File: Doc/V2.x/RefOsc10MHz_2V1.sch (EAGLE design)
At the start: 81 parts, among them CON1 TYCO-AMP_USBUSB-B_SMT, CON2 HEADER-2X5SMD, CON3 SD-73100-0105, CON4 AVR-ISP-6SMD, CON5 AVR-JTAG-10SMD, CON6 HEADER-2X3SMD, CON7 MCX-J-P-X-RA-SM1, IC1 ATmega328-P, IC2 LC4032V_XXT44, IC3 74HCT221D, IC6 LM2831YMF, IC7 CFPT-141, IC8 712-RXM-GNSS-TM-B, U5 OPA354

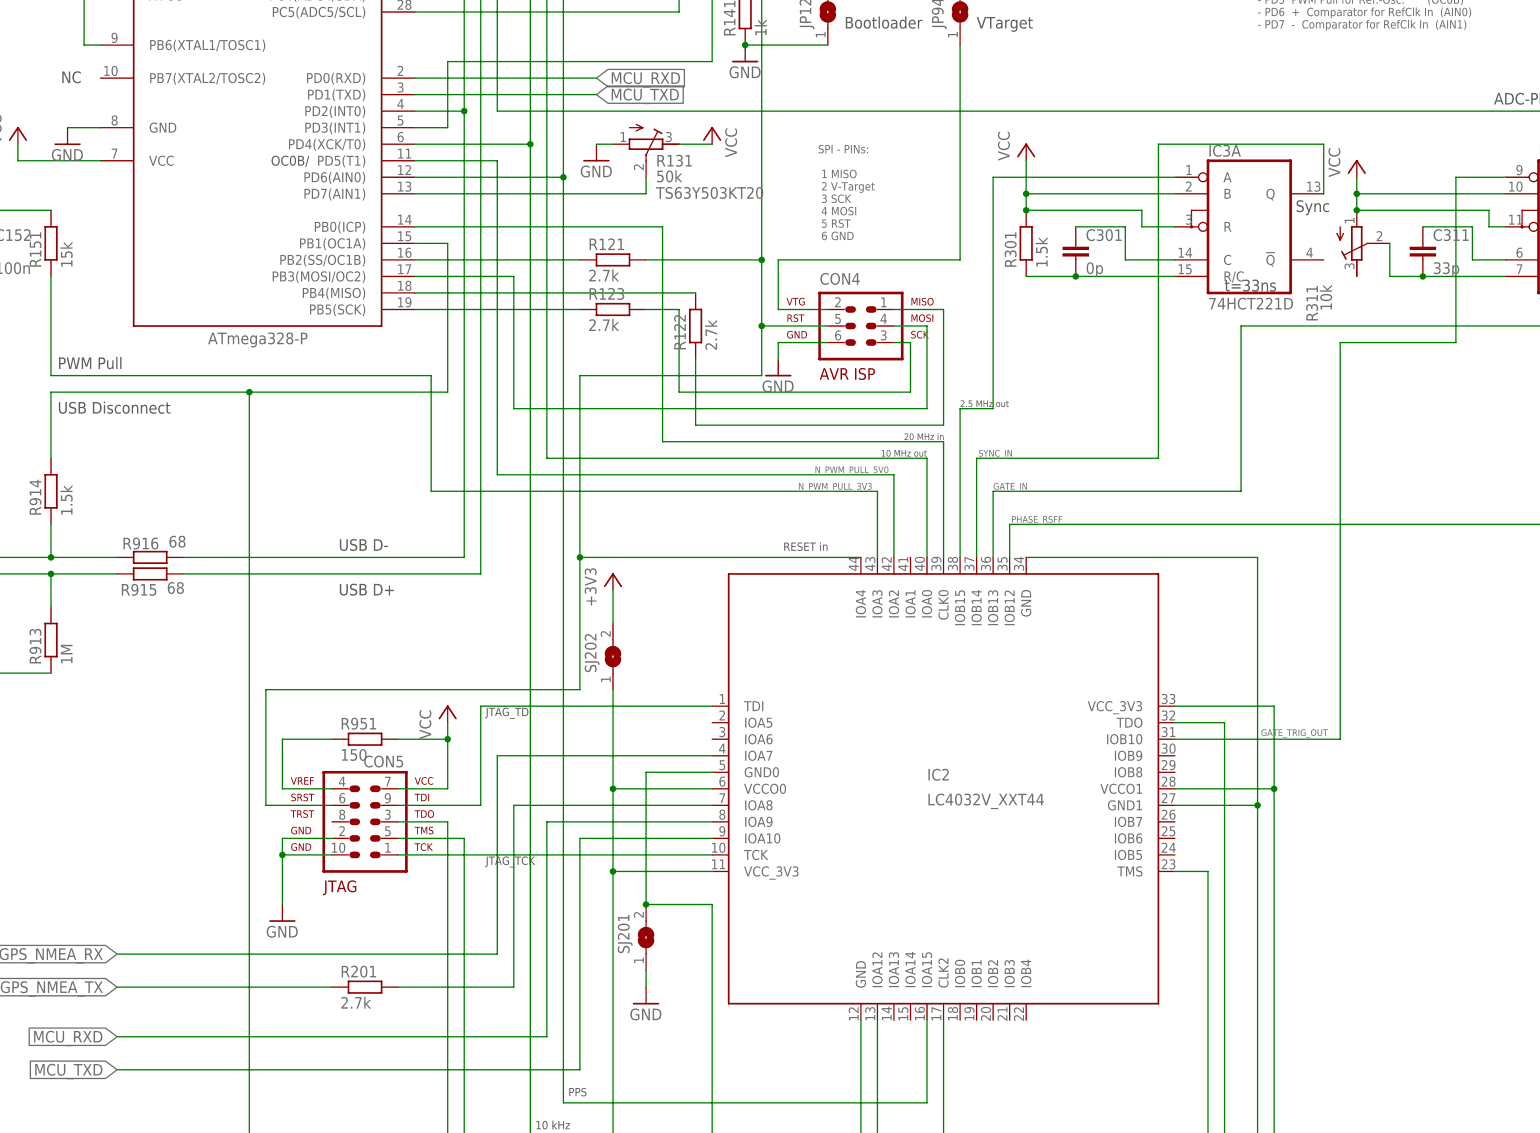
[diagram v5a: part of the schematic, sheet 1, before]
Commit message: avr_DF4IAH_Bootloader - Doc - Eagle: V2.1 - PWM pull signal via CPLD for clamping signals to defined values. AVR controller @ USB is not voltage regulated, the PWM output is therefore variable in its output voltage
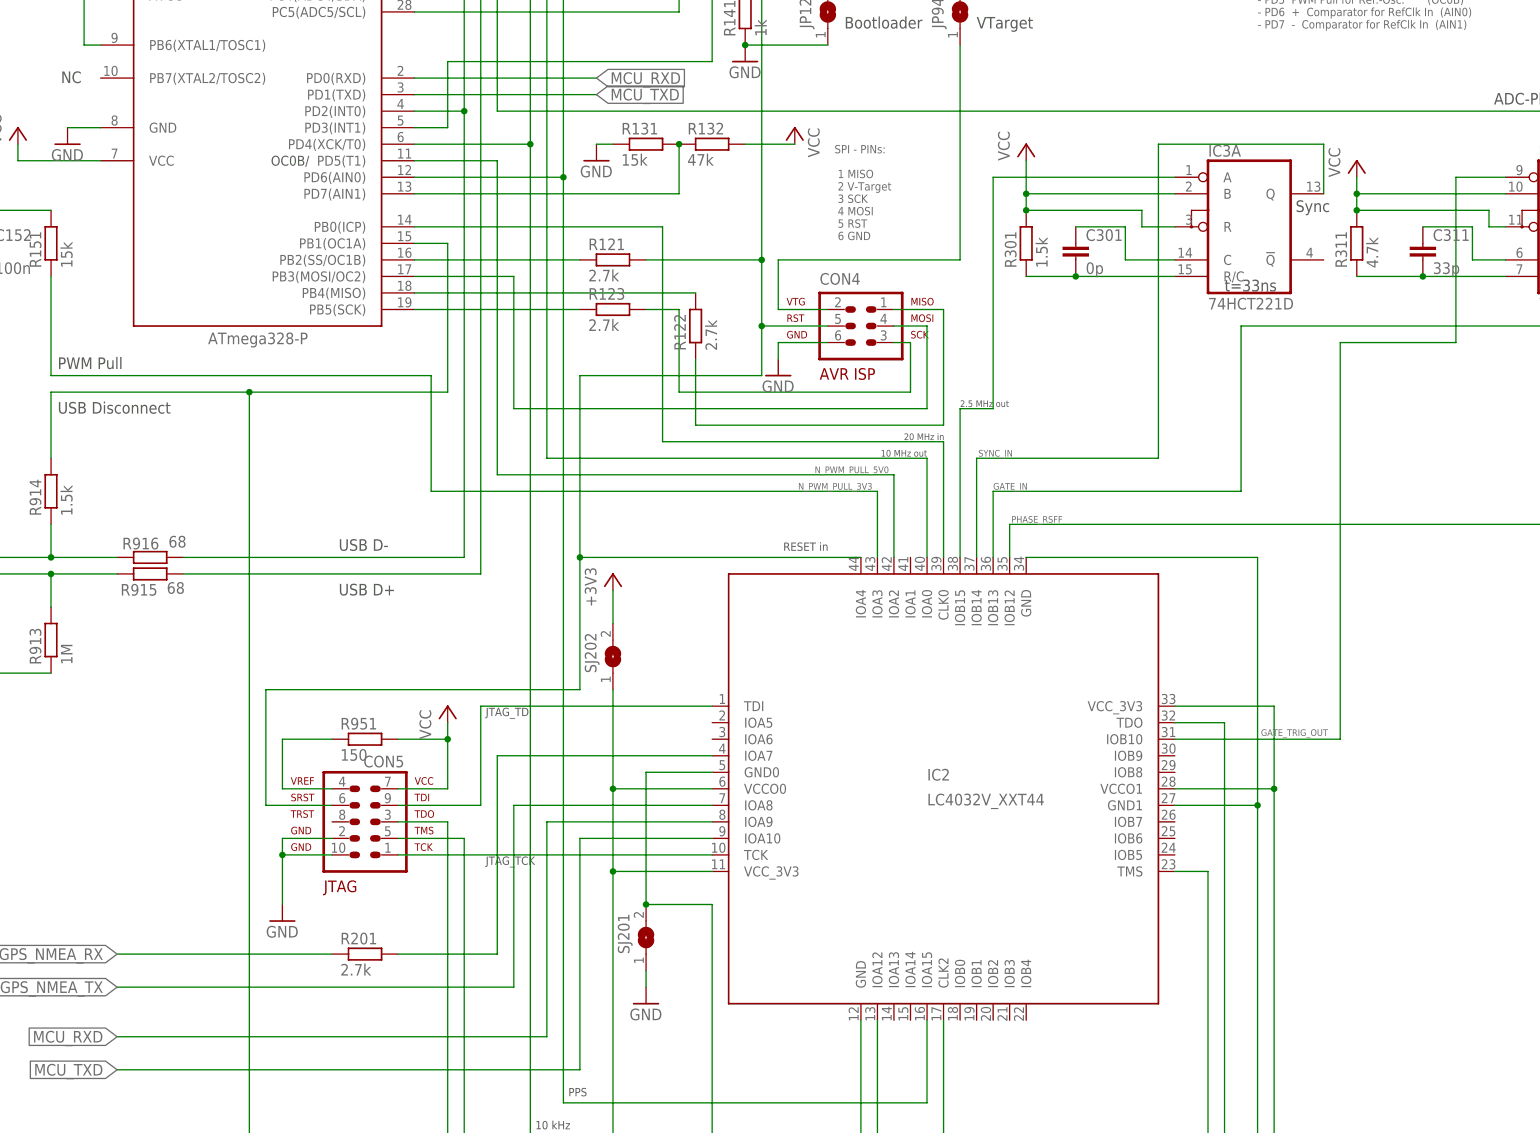
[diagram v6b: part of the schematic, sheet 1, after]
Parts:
- added R132: 47k, rcl:R-EU_R0805
- R131: value 50k -> 15k; device df4iah:R-TRIMMTS63Y -> rcl:R-EU_R0805; NR TS63Y503KT20 -> (none)
- R311: value 10k -> 4.7k; device df4iah:R-TRIMMTS63Y -> rcl:R-EU_R0805
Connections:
- removed net CPLD_GPS_NMEA_TX: IC2.IOA8, R201.2
- new net CPLD_GPS_NMEA_RX: IC2.IOA7, R201.2
- net AIN1: now also R131.2, R132.1; no longer R131.S
- net GND: now also R131.1; no longer R131.A
- net GPS_NMEA_RX: now also R201.1; no longer IC2.IOA7
- net GPS_NMEA_TX: now also IC2.IOA8; no longer R201.1
- net N$44: now also R311.1; no longer R311.S
- net VCC: now also R132.2, R311.2; no longer R131.E, R311.A
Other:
- moved on the sheet: R201
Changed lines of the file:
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@@
 <part name="JP941" library="jumper" deviceset="SJ" device="W"/>
 <part name="JP121" library="jumper" deviceset="SJ" device="W"/>
-<part name="R131" library="df4iah" deviceset="R-TRIMM" device="TS63Y" value="50k">
-<attribute name="NR" value="TS63Y503KT20"/>
-</part>
-<part name="R311" library="df4iah" deviceset="R-TRIMM" device="TS63Y" value="10k"/>
 <part name="GND6" library="supply1" deviceset="GND" device=""/>
 <part name="CON2" library="df4iah" deviceset="HEADER-2X5" device="SMD"/>
@@
 <part name="L101" library="rcl" deviceset="L-EU" device="L1812" value="10uH"/>
 <part name="IC6" library="df4iah" deviceset="LM2831" device="" technology="YMF" value="LM2831YMF"/>
-<part name="R201" library="rcl" deviceset="R-EU_" device="R0805" value="2.7k"/>
 <part name="GND12" library="supply1" deviceset="GND" device=""/>
 <part name="C791" library="rcl" deviceset="C-EU" device="C0805" value="100n"/>
@@
 <part name="R412" library="rcl" deviceset="R-EU_" device="R0805" value="2M"/>
 <part name="D401" library="diode" deviceset="DIODE-" device="SOD123" value="1N4448"/>
+<part name="R201" library="rcl" deviceset="R-EU_" device="R0805" value="2.7k"/>
+<part name="R131" library="rcl" deviceset="R-EU_" device="R0805" value="15k"/>
+<part name="R132" library="rcl" deviceset="R-EU_" device="R0805" value="47k"/>
+<part name="R311" library="rcl" deviceset="R-EU_" device="R0805" value="4.7k"/>
 </parts>
 <sheets>
@@
 <text x="107.696" y="89.916" size="1.778" layer="97">USB D-</text>
 <text x="107.696" y="83.058" size="1.778" layer="97">USB D+</text>
-<text x="181.356" y="137.668" size="1.27" layer="96" font="fixed">SPI - PINs:
+<text x="183.896" y="137.668" size="1.27" layer="96" font="fixed">SPI - PINs:
  1 MISO
  2 V-Target
@@
 <instance part="P+3" gate="VCC" x="10.16" y="251.46"/>
 <instance part="P+4" gate="VCC" x="203.2" y="182.88"/>
-<instance part="P+5" gate="VCC" x="165.1" y="154.94" smashed="yes">
-<attribute name="VALUE" x="168.91" y="150.368" size="1.778" layer="96" rot="R90"/>
+<instance part="P+5" gate="VCC" x="177.8" y="154.94" smashed="yes">
+<attribute name="VALUE" x="181.61" y="150.368" size="1.778" layer="96" rot="R90"/>
 </instance>
 <instance part="GND10" gate="1" x="170.18" y="165.1"/>
@@
 <instance part="JP941" gate="1" x="203.2" y="172.72" rot="R90"/>
 <instance part="JP121" gate="1" x="182.88" y="172.72" rot="R90"/>
-<instance part="R131" gate="G$1" x="154.94" y="152.4" smashed="yes" rot="R270">
-<attribute name="NR" x="156.464" y="144.018" size="1.778" layer="96"/>
-<attribute name="NAME" x="156.464" y="148.971" size="1.778" layer="95"/>
-<attribute name="VALUE" x="156.464" y="146.558" size="1.778" layer="96"/>
-</instance>
-<instance part="R311" gate="G$1" x="264.16" y="137.16" smashed="yes" rot="MR180">
-<attribute name="NAME" x="258.191" y="130.81" size="1.778" layer="95" rot="MR270"/>
-<attribute name="VALUE" x="260.35" y="130.81" size="1.778" layer="96" rot="MR270"/>
-</instance>
 <instance part="GND6" gate="1" x="175.26" y="116.84"/>
 <instance part="CON2" gate="G$1" x="210.82" y="215.9"/>
@@
 <instance part="L101" gate="G$1" x="38.1" y="175.26" rot="R270"/>
 <instance part="IC6" gate="A" x="35.56" y="238.76"/>
-<instance part="R201" gate="G$1" x="111.76" y="22.86"/>
 <instance part="GND12" gate="1" x="111.76" y="236.22"/>
 <instance part="C791" gate="G$1" x="96.52" y="238.76" smashed="yes" rot="R90">
@@
 <instance part="R412" gate="G$1" x="330.2" y="76.2" rot="R90"/>
 <instance part="D401" gate="G$1" x="307.34" y="93.98"/>
+<instance part="R201" gate="G$1" x="111.76" y="27.94"/>
+<instance part="R131" gate="G$1" x="154.94" y="152.4"/>
+<instance part="R132" gate="G$1" x="165.1" y="152.4"/>
+<instance part="R311" gate="G$1" x="264.16" y="137.16" rot="R90"/>
 </instances>
 <busses>
@@
 <pinref part="GND8" gate="1" pin="GND"/>
 <wire x1="147.32" y1="152.4" x2="149.86" y2="152.4" width="0.1524" layer="91"/>
-<pinref part="R131" gate="G$1" pin="A"/>
+<pinref part="R131" gate="G$1" pin="1"/>
 </segment>
 <segment>
@@
 <segment>
 <pinref part="P+5" gate="VCC" pin="VCC"/>
-<wire x1="165.1" y1="152.4" x2="160.02" y2="152.4" width="0.1524" layer="91"/>
-<pinref part="R131" gate="G$1" pin="E"/>
+<pinref part="R132" gate="G$1" pin="2"/>
+<wire x1="177.8" y1="152.4" x2="170.18" y2="152.4" width="0.1524" layer="91"/>
 </segment>
 <segment>
@@
 <wire x1="284.48" y1="142.24" x2="284.48" y2="139.7" width="0.1524" layer="91"/>
 <wire x1="284.48" y1="139.7" x2="287.02" y2="139.7" width="0.1524" layer="91"/>
-<pinref part="R311" gate="G$1" pin="A"/>
-<junction x="264.16" y="142.24"/>
 <pinref part="IC3" gate="B" pin="B"/>
 <pinref part="IC3" gate="B" pin="R"/>
+<pinref part="R311" gate="G$1" pin="2"/>
+<junction x="264.16" y="142.24"/>
 </segment>
 <segment>
@@
 </segment>
 <segment>
-<wire x1="106.68" y1="22.86" x2="73.66" y2="22.86" width="0.1524" layer="91"/>
+<wire x1="134.62" y1="22.86" x2="73.66" y2="22.86" width="0.1524" layer="91"/>
 <label x="73.66" y="22.86" size="1.778" layer="95" rot="R180" xref="yes"/>
-<pinref part="R201" gate="G$1" pin="1"/>
+<pinref part="IC2" gate="G$1" pin="IOA8"/>
+<wire x1="165.1" y1="50.8" x2="134.62" y2="50.8" width="0.1524" layer="91"/>
+<wire x1="134.62" y1="22.86" x2="134.62" y2="50.8" width="0.1524" layer="91"/>
 </segment>
 </net>
@@
 <segment>
 <pinref part="IC1" gate="G$1" pin="PD7(AIN1)"/>
-<wire x1="119.38" y1="144.78" x2="154.94" y2="144.78" width="0.1524" layer="91"/>
-<wire x1="154.94" y1="144.78" x2="154.94" y2="147.32" width="0.1524" layer="91"/>
-<pinref part="R131" gate="G$1" pin="S"/>
+<wire x1="119.38" y1="144.78" x2="160.02" y2="144.78" width="0.1524" layer="91"/>
+<pinref part="R131" gate="G$1" pin="2"/>
+<pinref part="R132" gate="G$1" pin="1"/>
+<wire x1="160.02" y1="144.78" x2="160.02" y2="152.4" width="0.1524" layer="91"/>
+<junction x="160.02" y="152.4"/>
 </segment>
 </net>
@@
 <net name="N$44" class="0">
 <segment>
-<wire x1="269.24" y1="132.08" x2="274.32" y2="132.08" width="0.1524" layer="91"/>
+<wire x1="264.16" y1="132.08" x2="274.32" y2="132.08" width="0.1524" layer="91"/>
 <wire x1="274.32" y1="132.08" x2="287.02" y2="132.08" width="0.1524" layer="91"/>
-<wire x1="269.24" y1="132.08" x2="269.24" y2="137.16" width="0.1524" layer="91"/>
-<pinref part="R311" gate="G$1" pin="S"/>
 <pinref part="IC3" gate="B" pin="R/C"/>
 <pinref part="C311" gate="G$1" pin="2"/>
 <junction x="274.32" y="132.08"/>
+<pinref part="R311" gate="G$1" pin="1"/>
 </segment>
 </net>
@@
 </segment>
 <segment>
-<pinref part="IC2" gate="G$1" pin="IOA7"/>
-<wire x1="165.1" y1="58.42" x2="132.08" y2="58.42" width="0.1524" layer="91"/>
-<wire x1="132.08" y1="58.42" x2="132.08" y2="27.94" width="0.1524" layer="91"/>
-<wire x1="132.08" y1="27.94" x2="73.66" y2="27.94" width="0.1524" layer="91"/>
+<wire x1="106.68" y1="27.94" x2="73.66" y2="27.94" width="0.1524" layer="91"/>
 <label x="73.66" y="27.94" size="1.778" layer="95" rot="R180" xref="yes"/>
+<pinref part="R201" gate="G$1" pin="1"/>
 </segment>
 </net>
@@
 </segment>
 </net>
-<net name="CPLD_GPS_NMEA_TX" class="0">
-<segment>
-<pinref part="IC2" gate="G$1" pin="IOA8"/>
-<wire x1="165.1" y1="50.8" x2="134.62" y2="50.8" width="0.1524" layer="91"/>
-<pinref part="R201" gate="G$1" pin="2"/>
-<wire x1="116.84" y1="22.86" x2="134.62" y2="22.86" width="0.1524" layer="91"/>
-<wire x1="134.62" y1="22.86" x2="134.62" y2="50.8" width="0.1524" layer="91"/>
-</segment>
-</net>
 <net name="+3V0" class="1">
 <segment>
@@
 </segment>
 </net>
+<net name="CPLD_GPS_NMEA_RX" class="0">
+<segment>
+<pinref part="IC2" gate="G$1" pin="IOA7"/>
+<wire x1="165.1" y1="58.42" x2="132.08" y2="58.42" width="0.1524" layer="91"/>
+<wire x1="132.08" y1="58.42" x2="132.08" y2="27.94" width="0.1524" layer="91"/>
+<wire x1="132.08" y1="27.94" x2="116.84" y2="27.94" width="0.1524" layer="91"/>
+<pinref part="R201" gate="G$1" pin="2"/>
+</segment>
+</net>
